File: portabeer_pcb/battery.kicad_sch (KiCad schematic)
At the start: 50 parts, among them J13 XT60IPW, J14 Barrel_Jack_MountingPin, Q3 BSS138, Q4 Si7145DP, Q5 Si7145DP, U10 LTC4412xS6, U11 MP26124, U9 LTC2943

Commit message: electronics diagram and schematic
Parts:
- C54, C60: footprint (none) -> Capacitor_THT:CP_Radial_D6.3mm_P2.50mm
- C57: footprint (none) -> Capacitor_THT:CP_Radial_D8.0mm_P3.50mm
- Q3: footprint Package_TO_SOT_SMD:SOT-523 -> Package_TO_SOT_SMD:SOT-23
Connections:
- net GND: no longer U9. (GND)
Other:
- note added: "Address: 1100100"
- note removed: "Address: 1100100 (0x64)"
- company: (none) -> ©2024 Luca Anastasio
- title: (none) -> Beerpak
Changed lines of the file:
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@@
 	(generator_version "8.0")
 	(paper "A4")
+	(title_block
+		(title "Beerpak")
+		(company "©2024 Luca Anastasio")
+	)
 	(junction
 		(at 171.45 109.22)
@@
 		)
 	)
-	(text "Address: 1100100 (0x64)"
+	(text "Address: 1100100"
 		(exclude_from_sim no)
 		(at 85.852 119.126 0)
@@
 		(pin "7"
 		)
-		(pin ""
-		)
 		(pin "9"
 		)
@@
 			)
 		)
-		(property "Datasheet" "https://www.vishay.com/docs/64814/si7145dp.pdf"
+		(property "Datasheet" "https://www.vishay.com/docs/65596/si7141dp.pdf"
 			(at 113.03 26.67 0)
 			(effects
@@
 			)
 		)
-		(property "Description" "-60A Id, -30V Vds, 2.6 mOhm Ron, PowerPAK-8"
+		(property "Description" "-60A Id, -20V Vds, 1.9 mOhm Ron, PowerPAK-8"
 			(at 109.22 31.75 0)
 			(effects
@@
 			)
 		)
-		(property "Footprint" ""
+		(property "Footprint" "Capacitor_THT:CP_Radial_D8.0mm_P3.50mm"
 			(at 216.8652 41.91 0)
 			(effects
@@
 			)
 		)
-		(property "Datasheet" "https://www.vishay.com/docs/64814/si7145dp.pdf"
+		(property "Datasheet" "https://www.vishay.com/docs/65596/si7141dp.pdf"
 			(at 130.81 26.67 0)
 			(effects
@@
 			)
 		)
-		(property "Description" "-60A Id, -30V Vds, 2.6 mOhm Ron, PowerPAK-8"
+		(property "Description" "-60A Id, -20V Vds, 1.9 mOhm Ron, PowerPAK-8"
 			(at 134.62 31.75 0)
 			(effects
@@
 			)
 		)
-		(property "Footprint" ""
+		(property "Footprint" "Capacitor_THT:CP_Radial_D6.3mm_P2.50mm"
 			(at 242.2652 41.91 0)
 			(effects
@@
 			)
 		)
-		(property "Footprint" ""
+		(property "Footprint" "Capacitor_THT:CP_Radial_D6.3mm_P2.50mm"
 			(at 191.4652 41.91 0)
 			(effects
@@
 			)
 		)
-		(property "Footprint" "Package_TO_SOT_SMD:SOT-523"
+		(property "Footprint" "Package_TO_SOT_SMD:SOT-23"
 			(at 46.355 96.52 0)
 			(effects

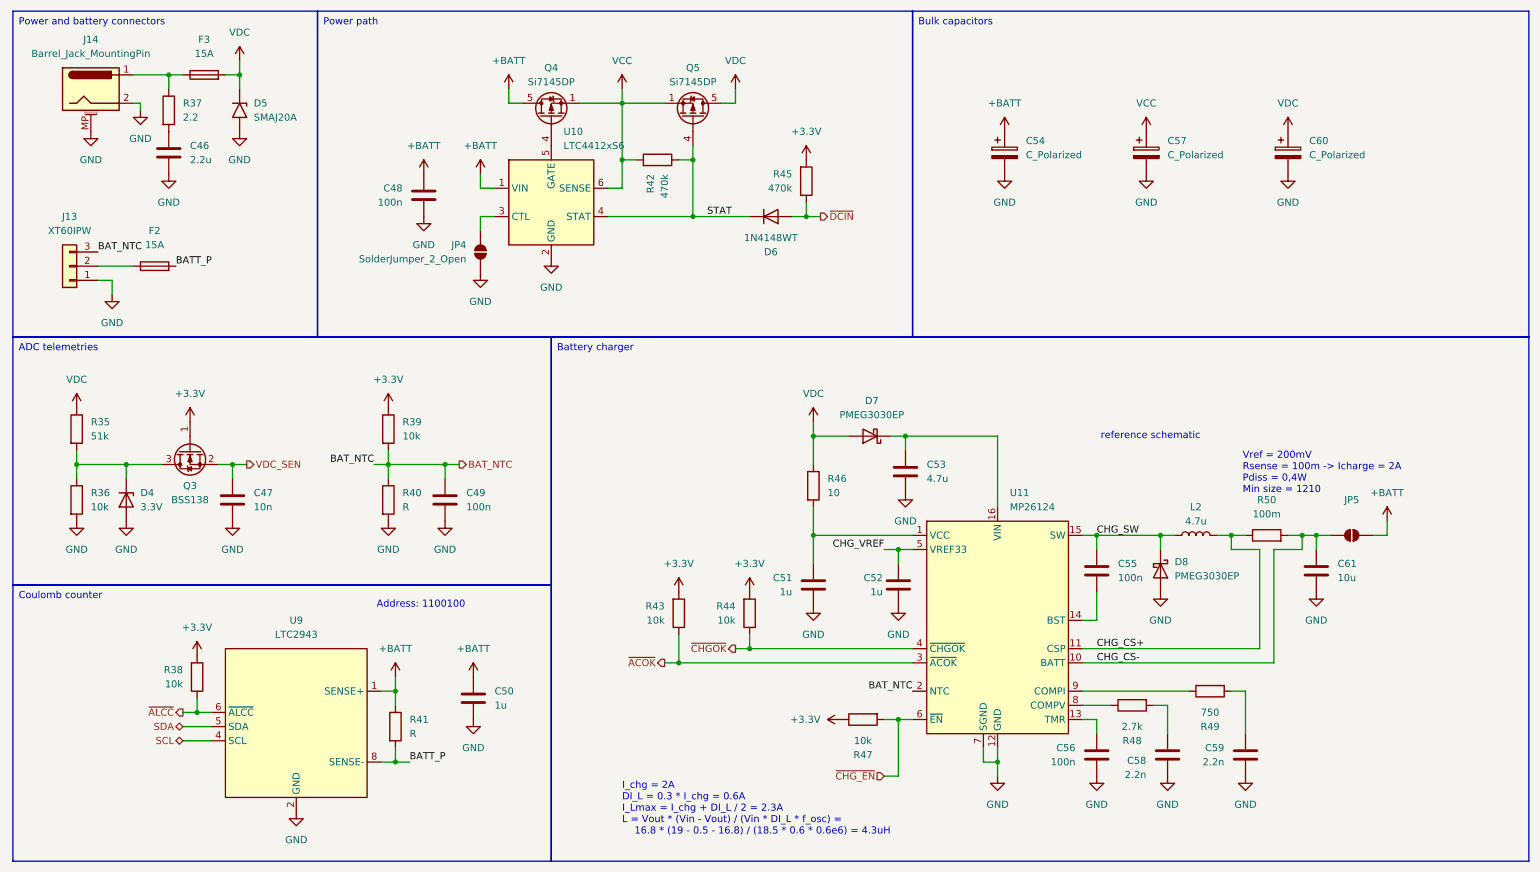
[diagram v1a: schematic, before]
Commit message: added 3d models, started layout
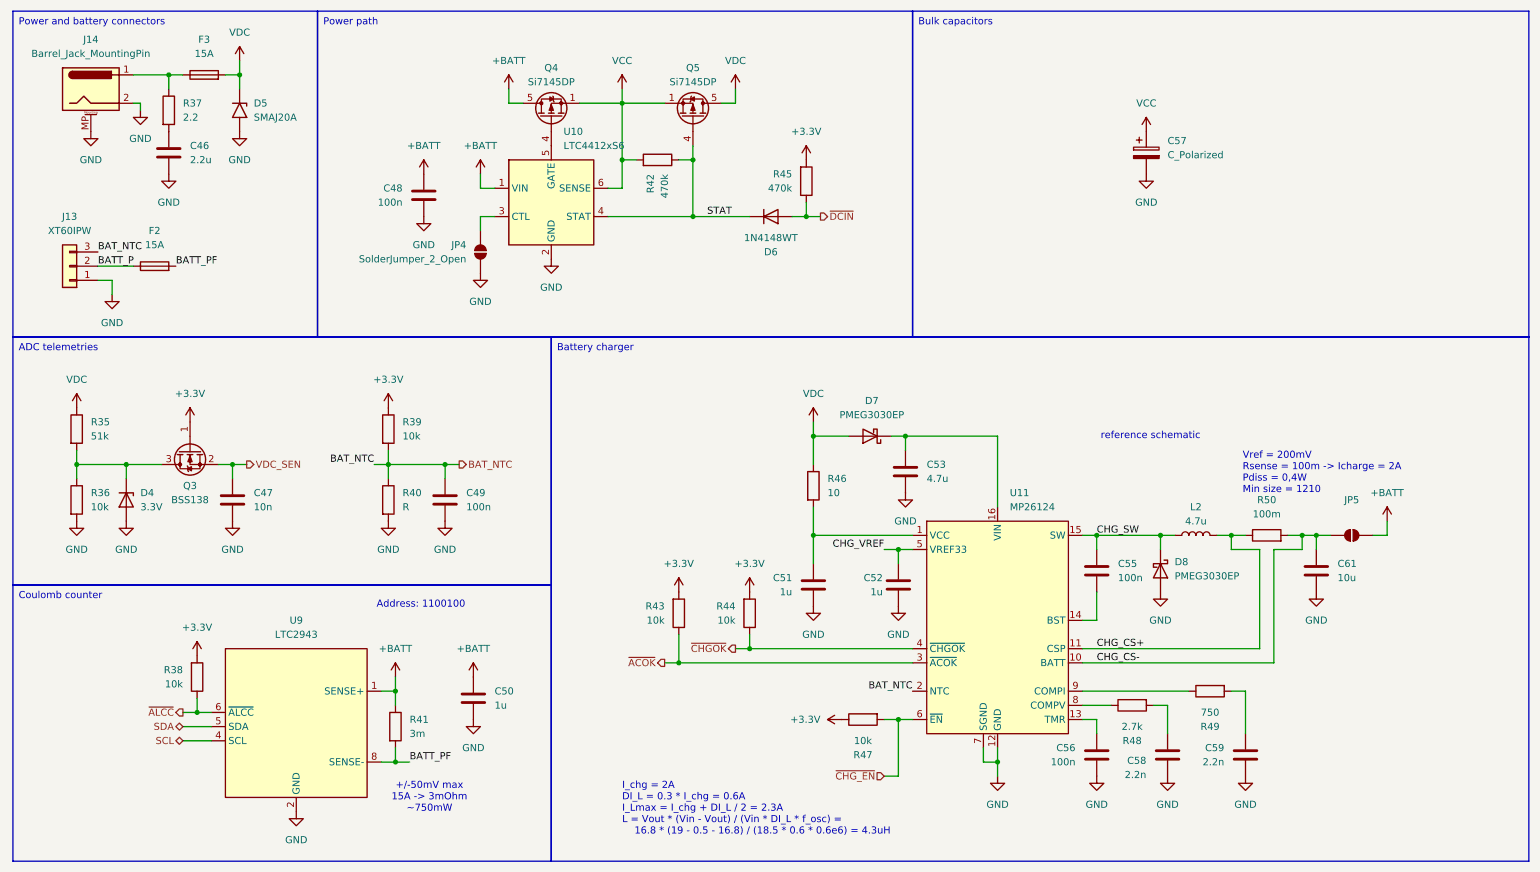
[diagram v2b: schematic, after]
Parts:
- removed C54, C60: C_Polarized, Capacitor_THT:CP_Radial_D6.3mm_P2.50mm, symbol Device:C_Polarized
- J13: footprint Connector_AMASS:AMASS_XT60IPW-M_1x03_P7.20mm_Horizontal -> portabeer:AMASS_XT60IPW-M_1x03_P7.20mm_Horizontal
- L2: footprint Inductor_SMD:L_Taiyo-Yuden_NR-50xx -> portabeer:L_Taiyo-Yuden_NR-50xx
- Q4, Q5: footprint Package_SO:PowerPAK_SO-8_Single -> portabeer:PowerPAK_SO-8_Single
- R41: value R -> 3m
- U9: footprint Package_DFN_QFN:DFN-8-1EP_3x3mm_P0.5mm_EP1.65x2.38mm -> portabeer:DFN-8-1EP_3x3mm_P0.5mm_EP1.65x2.38mm
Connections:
- net BATT_P: now also F2.1, J13.2 (Pin_2); no longer F2.2, R41.2, U9.8 (SENSE-)
- new net BATT_PF: F2.2, R41.2, U9.8 (SENSE-)
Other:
- note added: "+/-50mV max 15A -> 3mOhm ~750mW"

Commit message: layout
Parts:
- added HS3: Heatsink, portabeer:Heatsink_9x9x5mm_adhesive, symbol Mechanical:Heatsink
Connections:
- net VDC_UF: now reaches F3.1, J14.1, R37.1
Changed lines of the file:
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@@
 		)
 	)
+	(label "VDC_UF"
+		(at 34.29 24.13 0)
+		(fields_autoplaced yes)
+		(effects
+			(font
+				(size 1.27 1.27)
+			)
+			(justify left bottom)
+		)
+	)
 	(label "BATT_PF"
 		(at 83.82 147.32 0)
@@
 					(unit 1)
 				)
+			)
+		)
+	)
+	(symbol
+		(lib_id "Mechanical:Heatsink")
+		(at 215.9 81.28 0)
+		(unit 1)
+		(exclude_from_sim yes)
+		(in_bom yes)
+		(on_board yes)
+		(dnp no)
+		(fields_autoplaced yes)
+		(property "Reference" "HS3"
+			(at 219.71 78.1049 0)
+			(effects
+				(font
+					(size 1.27 1.27)
+				)
+				(justify left)
+			)
+		)
+		(property "Value" "Heatsink"
+			(at 219.71 80.6449 0)
+			(effects
+				(font
+					(size 1.27 1.27)
+				)
+				(justify left)
+			)
+		)
+		(property "Footprint" "portabeer:Heatsink_9x9x5mm_adhesive"
+			(at 216.2048 81.28 0)
+			(effects
+				(font
+					(size 1.27 1.27)
+				)
+				(hide yes)
+			)
+		)
+		(property "Datasheet" "~"
+			(at 216.2048 81.28 0)
+			(effects
+				(font
+					(size 1.27 1.27)
+				)
+				(hide yes)
+			)
+		)
+		(property "Description" "Heatsink"
+			(at 215.9 81.28 0)
+			(effects
+				(font
+					(size 1.27 1.27)
+				)
+				(hide yes)
+			)
+		)
+		(instances
+			(project "portabeer_pcb"
+				(path "/bb676e84-aa44-417a-9a70-748af1c322fb/1d31c221-9102-4c6e-88ae-84173ddae6a8"
+					(reference "HS3")
+					(unit 1)
+				)

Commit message: working
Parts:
- added R68: 0, Resistor_SMD:R_0603_1608Metric, symbol Device:R
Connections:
- net BAT_NTC: now also R68.1; no longer U11.2 (NTC)
- new net: R68.2, U11.2 (NTC)
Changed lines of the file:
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@@
 	(wire
 		(pts
+			(xy 149.86 134.62) (xy 173.99 134.62)
+		)
+		(stroke
+			(width 0)
+			(type default)
+		)
+	)
+	(wire
+		(pts
 			(xy 259.08 104.14) (xy 259.08 106.68)
 		)
@@
 	)
 	(label "BAT_NTC"
-		(at 173.99 134.62 180)
+		(at 142.24 134.62 180)
 		(fields_autoplaced yes)
 		(effects
@@
 					(unit 1)
 				)
+			)
+		)
+	)
+	(symbol
+		(lib_id "Device:R")
+		(at 146.05 134.62 90)
+		(mirror x)
+		(unit 1)
+		(exclude_from_sim no)
+		(in_bom yes)
+		(on_board yes)
+		(dnp no)
+		(property "Reference" "R68"
+			(at 146.05 140.97 90)
+			(effects
+				(font
+					(size 1.27 1.27)
+				)
+			)
+		)
+		(property "Value" "0"
+			(at 146.05 138.43 90)
+			(effects
+				(font
+					(size 1.27 1.27)
+				)
+			)
+		)
+		(property "Footprint" "Resistor_SMD:R_0603_1608Metric"
+			(at 146.05 132.842 90)
+			(effects
+				(font
+					(size 1.27 1.27)
+				)
+				(hide yes)
+			)
+		)
+		(property "Datasheet" "~"
+			(at 146.05 134.62 0)
+			(effects
+				(font
+					(size 1.27 1.27)
+				)
+				(hide yes)
+			)
+		)
+		(property "Description" "Resistor"
+			(at 146.05 134.62 0)
+			(effects
+				(font
+					(size 1.27 1.27)
+				)
+				(hide yes)
+			)
+		)
+		(pin "2"
+		)
+		(pin "1"
+		)
+		(instances
+			(project "portabeer_pcb"
+				(path "/bb676e84-aa44-417a-9a70-748af1c322fb/1d31c221-9102-4c6e-88ae-84173ddae6a8"
+					(reference "R68")
+					(unit 1)
+				)

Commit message: partial routing
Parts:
- C57: footprint Capacitor_THT:CP_Radial_D8.0mm_P3.50mm -> Capacitor_THT:CP_Radial_D6.3mm_P2.50mm
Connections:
- net VDC_SCAL: now reaches D4.1 (K), Q3.3 (D), R35.2, R36.1
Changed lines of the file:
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@@
 (kicad_sch
-	(version 20231120)
+	(version 20250114)
 	(generator "eeschema")
-	(generator_version "8.0")
+	(generator_version "9.0")
 	(paper "A4")
 	(title_block
@@
 		(company "©2024 Luca Anastasio")
 	)
+	(text "I_chg = 2A\nDI_L = 0.3 * I_chg = 0.6A\nI_Lmax = I_chg + DI_L / 2 = 2.3A\nL = Vout * (Vin - Vout) / (Vin * DI_L * f_osc) =\n	16.8 * (19 - 0.5 - 16.8) / (18.5 * 0.6 * 0.6e6) = 4.3uH"
+		(exclude_from_sim no)
+		(at 121.92 150.876 0)
+		(effects
+			(font
+				(size 1.27 1.27)
+			)
+			(justify left top)
+		)
+	)
+	(text "reference schematic"
+		(exclude_from_sim no)
+		(at 216.662 88.9 0)
+		(effects
+			(font
+				(size 1.27 1.27)
+			)
+			(href "https://www.monolithicpower.com/en/documentview/productdocument/index/version/2/document_type/Datasheet/lang/en/sku/EV26124-R-00A/document_id/2872/")
+		)
+	)
+	(text "Address: 1100100"
+		(exclude_from_sim no)
+		(at 85.852 119.126 0)
+		(effects
+			(font
+				(size 1.27 1.27)
+			)
+		)
+	)
+	(text "+/-50mV max\n15A -> 3mOhm\n~750mW"
+		(exclude_from_sim no)
+		(at 87.376 153.67 0)
+		(effects
+			(font
+				(size 1.27 1.27)
+			)
+		)
+	)
+	(text "Vref = 200mV\nRsense = 100m -> Icharge = 2A\nPdiss = 0,4W\nMin size = 1210"
+		(exclude_from_sim no)
+		(at 233.172 91.694 0)
+		(effects
+			(font
+				(size 1.27 1.27)
+			)
+			(justify left top)
+		)
+	)
+	(text_box "ADC telemetries"
+		(exclude_from_sim no)
+		(at 12.7 71.12 0)
+		(size 96.52 44.45)
+		(margins 0.9525 0.9525 0.9525 0.9525)
+		(stroke
+			(width 0)
+			(type default)
+		)
+		(fill
+			(type none)
+		)
+		(effects
+			(font
+				(size 1.27 1.27)
+			)
+			(justify left top)
+		)
+	)
+	(text_box "Coulomb counter"
+		(exclude_from_sim no)
+		(at 12.7 115.57 0)
+		(size 96.52 49.53)
+		(margins 0.9525 0.9525 0.9525 0.9525)
+		(stroke
+			(width 0)
+			(type default)
+		)
+		(fill
+			(type none)
+		)
+		(effects
+			(font
+				(size 1.27 1.27)
+			)
+			(justify left top)
+		)
+	)
+	(text_box "Power path"
+		(exclude_from_sim no)
+		(at 67.31 12.7 0)
+		(size 106.68 58.42)
+		(margins 0.9525 0.9525 0.9525 0.9525)
+		(stroke
+			(width 0)
+			(type default)
+		)
+		(fill
+			(type none)
+		)
+		(effects
+			(font
+				(size 1.27 1.27)
+			)
+			(justify left top)
+		)
+	)
+	(text_box "Bulk capacitors"
+		(exclude_from_sim no)
+		(at 173.99 12.7 0)
+		(size 110.49 58.42)
+		(margins 0.9525 0.9525 0.9525 0.9525)
+		(stroke
+			(width 0)
+			(type default)
+		)
+		(fill
+			(type none)
+		)
+		(effects
+			(font
+				(size 1.27 1.27)
+			)
+			(justify left top)
+		)
+	)
+	(text_box "Power and battery connectors"
+		(exclude_from_sim no)
+		(at 12.7 12.7 0)
+		(size 54.61 58.42)
+		(margins 0.9525 0.9525 0.9525 0.9525)
+		(stroke
+			(width 0)
+			(type default)
+		)
+		(fill
+			(type none)
+		)
+		(effects
+			(font
+				(size 1.27 1.27)
+			)
+			(justify left top)
+		)
+	)
+	(text_box "Battery charger"
+		(exclude_from_sim no)
+		(at 109.22 71.12 0)
+		(size 175.26 93.98)
+		(margins 0.9525 0.9525 0.9525 0.9525)
+		(stroke
+			(width 0)
+			(type default)
+		)
+		(fill
+			(type none)
+		)
+		(effects
+			(font
+				(size 1.27 1.27)
+			)
+			(justify left top)
+		)
+	)
 	(junction
 		(at 171.45 109.22)
@@
 		)
 	)
-	(text_box "ADC telemetries"
-		(exclude_from_sim no)
-		(at 12.7 71.12 0)
-		(size 96.52 44.45)
-		(stroke
-			(width 0)
-			(type default)
-		)
-		(fill
-			(type none)
-		)
-		(effects
-			(font
-				(size 1.27 1.27)
-			)
-			(justify left top)
-		)
-	)
-	(text_box "Coulomb counter"
-		(exclude_from_sim no)
-		(at 12.7 115.57 0)
-		(size 96.52 49.53)
-		(stroke
-			(width 0)
-			(type default)
-		)
-		(fill
-			(type none)
-		)
-		(effects
-			(font
-				(size 1.27 1.27)
-			)
-			(justify left top)
-		)
-	)
-	(text_box "Power path"
-		(exclude_from_sim no)
-		(at 67.31 12.7 0)
-		(size 106.68 58.42)
-		(stroke
-			(width 0)
-			(type default)
-		)
-		(fill
-			(type none)
-		)
-		(effects
-			(font
-				(size 1.27 1.27)
-			)
-			(justify left top)
-		)
-	)
-	(text_box "Bulk capacitors"
-		(exclude_from_sim no)
-		(at 173.99 12.7 0)
-		(size 110.49 58.42)
-		(stroke
-			(width 0)
-			(type default)
-		)
-		(fill
-			(type none)
-		)
-		(effects
-			(font
-				(size 1.27 1.27)
-			)
-			(justify left top)
-		)
-	)
-	(text_box "Power and battery connectors"
-		(exclude_from_sim no)
-		(at 12.7 12.7 0)
-		(size 54.61 58.42)
-		(stroke
-			(width 0)
-			(type default)
-		)
-		(fill
-			(type none)
-		)
-		(effects
-			(font
-				(size 1.27 1.27)
-			)
-			(justify left top)
-		)
-	)
-	(text_box "Battery charger"
-		(exclude_from_sim no)
-		(at 109.22 71.12 0)
-		(size 175.26 93.98)
-		(stroke
-			(width 0)
-			(type default)
-		)
-		(fill
-			(type none)
-		)
-		(effects
-			(font
-				(size 1.27 1.27)
-			)
-			(justify left top)
-		)
-	)
-	(text "I_chg = 2A\nDI_L = 0.3 * I_chg = 0.6A\nI_Lmax = I_chg + DI_L / 2 = 2.3A\nL = Vout * (Vin - Vout) / (Vin * DI_L * f_osc) =\n	16.8 * (19 - 0.5 - 16.8) / (18.5 * 0.6 * 0.6e6) = 4.3uH"
-		(exclude_from_sim no)
-		(at 121.92 150.876 0)
-		(effects
-			(font
-				(size 1.27 1.27)
-			)
-			(justify left top)
-		)
-	)
-	(text "reference schematic"
-		(exclude_from_sim no)
-		(at 216.662 88.9 0)
-		(effects
-			(font
-				(size 1.27 1.27)
-			)
-			(href "https://www.monolithicpower.com/en/documentview/productdocument/index/version/2/document_type/Datasheet/lang/en/sku/EV26124-R-00A/document_id/2872/")
-		)
-	)
-	(text "Address: 1100100"
-		(exclude_from_sim no)
-		(at 85.852 119.126 0)
-		(effects
-			(font
-				(size 1.27 1.27)
-			)
-		)
-	)
-	(text "+/-50mV max\n15A -> 3mOhm\n~750mW"
-		(exclude_from_sim no)
-		(at 87.376 153.67 0)
-		(effects
-			(font
-				(size 1.27 1.27)
-			)
-		)
-	)
-	(text "Vref = 200mV\nRsense = 100m -> Icharge = 2A\nPdiss = 0,4W\nMin size = 1210"
-		(exclude_from_sim no)
-		(at 233.172 91.694 0)
-		(effects
-			(font
-				(size 1.27 1.27)
-			)
-			(justify left top)
-		)
-	)
 	(label "BAT_NTC"
 		(at 142.24 134.62 180)
-		(fields_autoplaced yes)
 		(effects
 			(font
@@
 	(label "CHG_CS-"
 		(at 207.01 129.54 0)
-		(fields_autoplaced yes)
 		(effects
 			(font
@@
 	(label "VDC_UF"
 		(at 34.29 24.13 0)
-		(fields_autoplaced yes)
 		(effects
 			(font
@@
 	(label "BATT_PF"
 		(at 83.82 147.32 0)
-		(fields_autoplaced yes)
 		(effects
 			(font
@@
 	(label "BATT_P"
 		(at 27.94 58.42 0)
-		(fields_autoplaced yes)
 		(effects
 			(font
@@
 	(label "BAT_NTC"
 		(at 77.47 93.98 180)
-		(fields_autoplaced yes)
 		(effects
 			(font
@@
 	(label "CHG_VREF"
 		(at 168.91 109.22 180)
-		(fields_autoplaced yes)
 		(effects
 			(font
@@
 	(label "STAT"
 		(at 137.16 49.53 0)
-		(fields_autoplaced yes)
 		(effects
 			(font
@@
 	(label "BAT_NTC"
 		(at 27.94 55.88 0)
-		(fields_autoplaced yes)
 		(effects
 			(font
@@
 	(label "CHG_SW"
 		(at 207.01 106.68 0)
-		(fields_autoplaced yes)
+		(effects
+			(font
+				(size 1.27 1.27)
+			)
+			(justify left bottom)
+		)
+	)
+	(label "VDC_SCAL"
+		(at 24.13 93.98 0)
 		(effects
 			(font
@@
 	(label "CHG_CS+"
 		(at 207.01 127 0)
-		(fields_autoplaced yes)
 		(effects
 			(font
@@
 	(label "BATT_PF"
 		(at 41.91 58.42 0)
-		(fields_autoplaced yes)
 		(effects
 			(font
@@
 		(shape output)
 		(at 92.71 93.98 0)
-		(fields_autoplaced yes)
 		(effects
 			(font
@@
 		(shape output)
 		(at 54.61 93.98 0)
-		(fields_autoplaced yes)
 		(effects
 			(font
@@
 		(shape output)
 		(at 157.48 49.53 0)
-		(fields_autoplaced yes)
 		(effects
 			(font
@@
 		(shape bidirectional)
 		(at 43.18 140.97 180)
-		(fields_autoplaced yes)
 		(effects
 			(font
@@
 		(shape output)
 		(at 43.18 138.43 180)
-		(fields_autoplaced yes)
 		(effects
 			(font
@@
 		(shape output)
 		(at 142.24 127 180)
-		(fields_autoplaced yes)
 		(effects
 			(font
@@
 		(shape output)
 		(at 129.54 129.54 180)
-		(fields_autoplaced yes)
 		(effects
 			(font
@@
 		(shape bidirectional)
 		(at 43.18 143.51 180)
-		(fields_autoplaced yes)
 		(effects
 			(font
@@
 		(shape input)
 		(at 168.91 149.86 180)
-		(fields_autoplaced yes)
 		(effects
 			(font
@@
 			)
 		)
-		(property "Footprint" "Capacitor_THT:CP_Radial_D8.0mm_P3.50mm"
+		(property "Footprint" "Capacitor_THT:CP_Radial_D6.3mm_P2.50mm"
 			(at 216.8652 41.91 0)
 			(effects
